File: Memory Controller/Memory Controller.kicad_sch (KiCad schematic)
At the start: 20 parts, among them J1 Conn_01x06, J2 Conn_01x02, U1 74AHC1G32, U2 74AHC1G04, U3 74AHC1G32, U4 74AHC1G32, U5 74AHC1G32, U6 74AHC1G04, U7 74AHC1G32, U8 74AHC1G32, U9 74AHC1G32

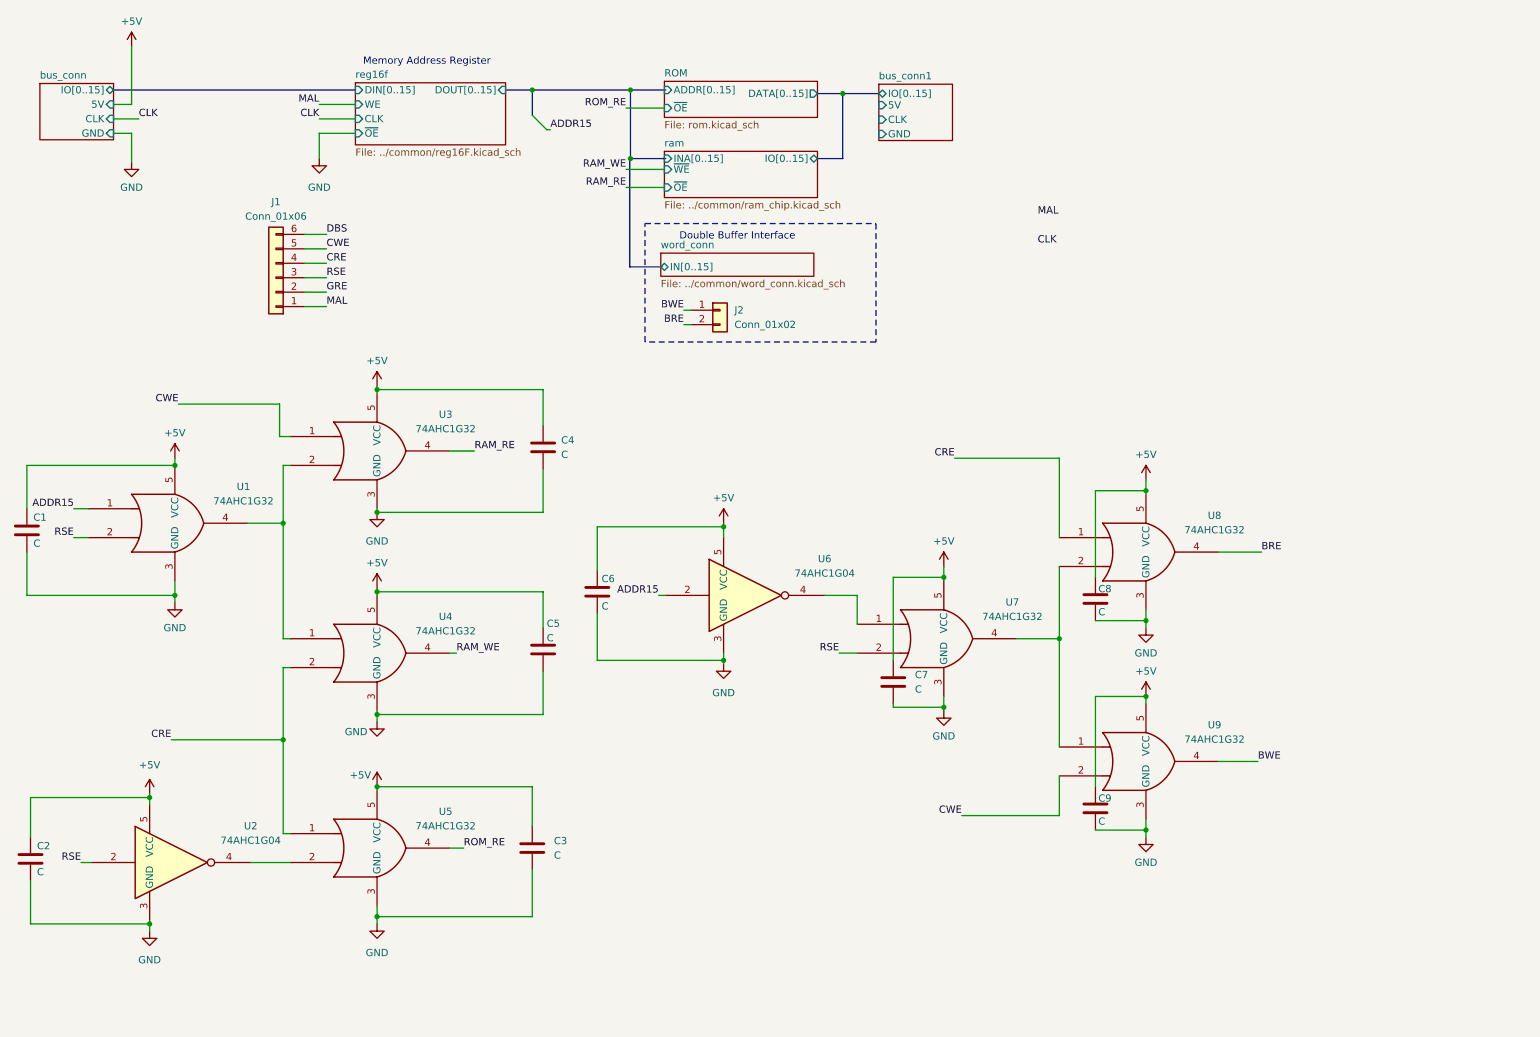
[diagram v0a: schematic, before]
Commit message: Memory Controller first draft
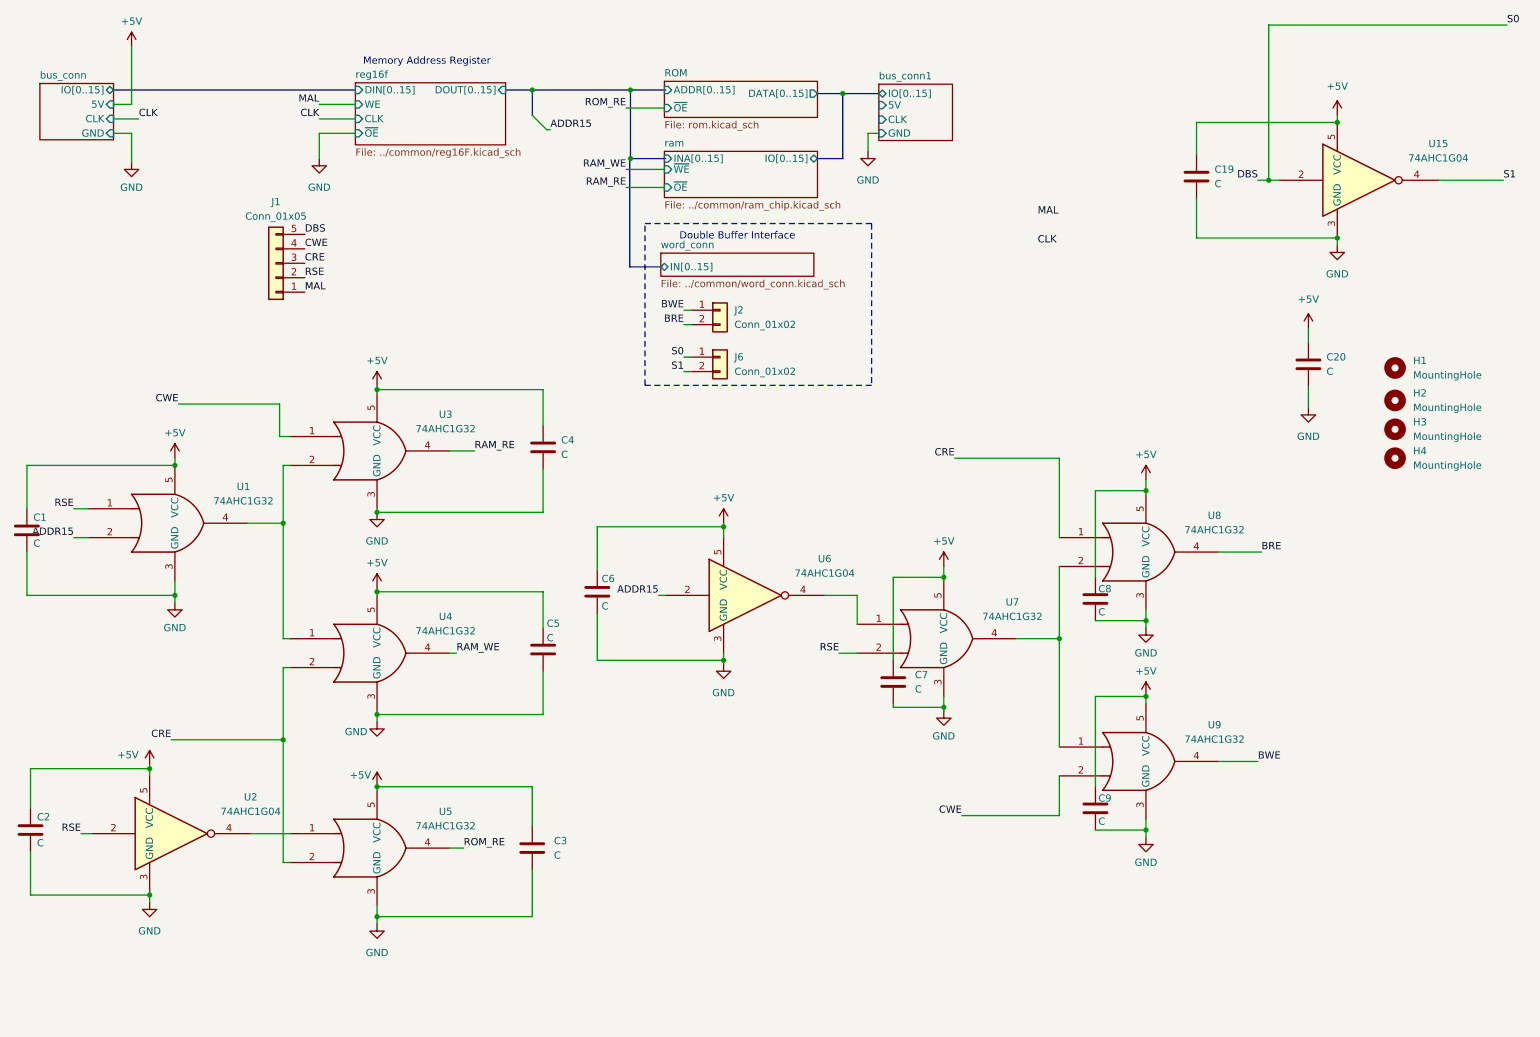
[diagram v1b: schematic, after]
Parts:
- removed J1: Conn_01x06, Connector_PinHeader_2.54mm:PinHeader_1x06_P2.54mm_Vertical, symbol Connector_Generic:Conn_01x06
- added C19: C, Capacitor_SMD:C_0603_1608Metric, symbol Device:C
- added C20: C, Capacitor_SMD:CP_Elec_5x5.3, symbol Device:C
- added H1, H2, H3, H4: MountingHole, MountingHole:MountingHole_4mm, symbol Mechanical:MountingHole
- added J1: Conn_01x05, Connector_PinHeader_2.54mm:PinHeader_1x05_P2.54mm_Vertical, symbol Connector_Generic:Conn_01x05
- added J6: Conn_01x02, Connector_PinHeader_2.54mm:PinHeader_1x02_P2.54mm_Vertical, symbol Connector_Generic:Conn_01x02
- added U15: 74AHC1G04, Package_TO_SOT_SMD:SOT-23-5, symbol 74xGxx:74AHC1G04
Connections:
- net +5V: now also C19.1, C20.1, U15.5 (VCC)
- net ADDR15: now also U1.2; no longer U1.1
- net CRE: now also U5.2, J1.3 (Pin_3); no longer U5.1
- net CWE: now also J1.4 (Pin_4)
- net DBS: now also J1.5 (Pin_5), J6.1 (Pin_1), U15.2
- net GND: now also C19.2, C20.2, U15.3 (GND)
- net MAL: now also J1.1 (Pin_1)
- net RSE: now also U1.1, J1.2 (Pin_2); no longer U1.2
- net at U2.4: now also U5.1; no longer U5.2
- new net S1: J6.2 (Pin_2), U15.4
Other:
- moved on the sheet: C2, U2

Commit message: Memory Controller fabrication checks complete
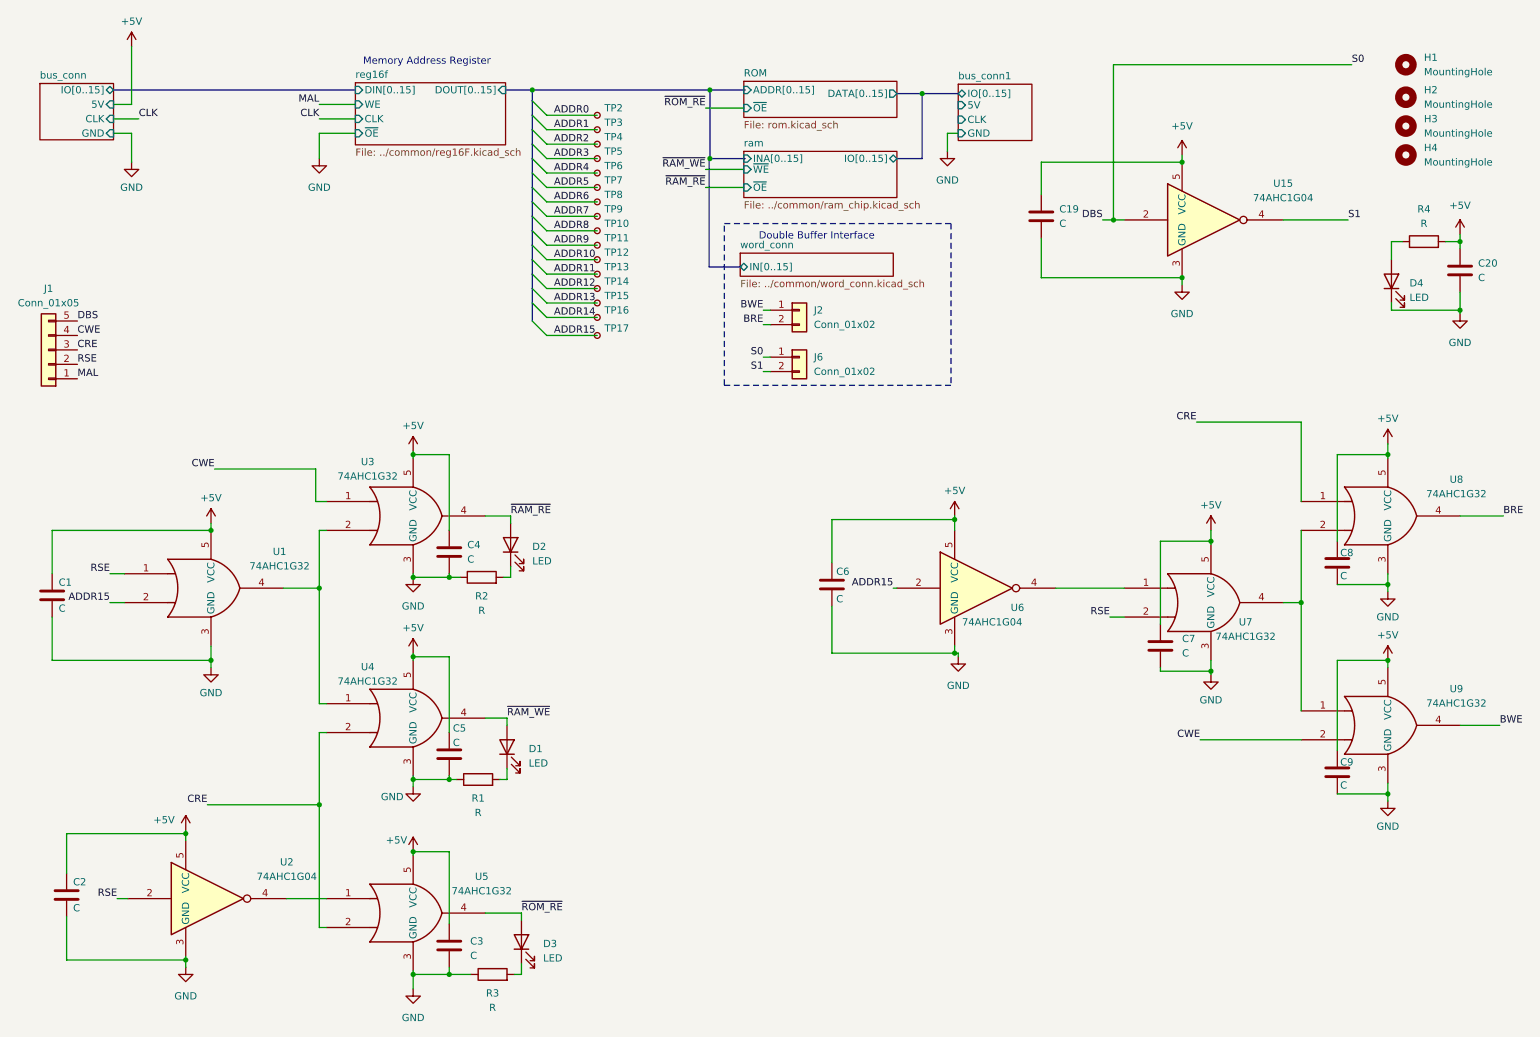
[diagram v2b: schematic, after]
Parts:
- added D1, D2, D3, D4: LED, LED_SMD:LED_0603_1608Metric, symbol Device:LED
- added R1, R2, R3, R4: R, Resistor_SMD:R_0603_1608Metric, symbol Device:R
- added TP10, TP11, TP12, TP13, TP14, TP15, TP16, TP17, TP2, TP3, TP4, TP5, TP6, TP7, TP8, TP9: TestPoint_Small, TestPoint:TestPoint_Pad_1.0x1.0mm, symbol Connector:TestPoint_Small
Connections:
- net +5V: now also R4.2
- net ADDR15: now also TP17.1
- net GND: now also D4.1 (K), R1.1, R2.1, R3.1
- net RAM_RE renamed ~{RAM_RE}
- net ~{RAM_RE}: now also D2.2 (A)
- net RAM_WE renamed ~{RAM_WE}
- net ~{RAM_WE}: now also D1.2 (A)
- net ROM_RE renamed ~{ROM_RE}
- net ~{ROM_RE}: now also D3.2 (A)
- new net: D3.1 (K), R3.2
- new net: D1.1 (K), R1.2
- new net: D2.1 (K), R2.2
- new net: D4.2 (A), R4.1
- new net ADDR0: TP2.1
- new net ADDR1: TP3.1
- new net ADDR10: TP12.1
- new net ADDR11: TP13.1
- new net ADDR12: TP14.1
- new net ADDR13: TP15.1
- new net ADDR14: TP16.1
- new net ADDR2: TP4.1
- new net ADDR3: TP5.1
- new net ADDR4: TP6.1
- new net ADDR5: TP7.1
- new net ADDR6: TP8.1
- new net ADDR7: TP9.1
- new net ADDR8: TP10.1
- new net ADDR9: TP11.1
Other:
- moved on the sheet: C1, C19, C2, C20, C3, C4, C5, C6, C7, C8, C9, H1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

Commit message: Control Unit first draft
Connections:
- net ~{RAM_RE}: now also D1.2 (A), U4.4; no longer D2.2 (A), U3.4
- net ~{RAM_WE}: now also D2.2 (A), U3.4; no longer D1.2 (A), U4.4
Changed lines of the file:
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@@
 		)
 	)
-	(label "~{RAM_WE}"
+	(label "~{RAM_RE}"
 		(at 99.695 137.795 0)
 		(effects
@@
 		)
 	)
-	(label "~{RAM_RE}"
+	(label "~{RAM_WE}"
 		(at 100.33 102.235 0)
 		(effects
